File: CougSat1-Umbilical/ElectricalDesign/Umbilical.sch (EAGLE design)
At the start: 42 parts, among them J3 5V input, Q1 CSD16406Q3, Q2 CSD16406Q3, U1 FT230XQ, U2 BQ24650

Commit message: added test points
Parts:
- added TP1, TP2, TP3, TP4, TP5, TP6, TP7: TEST_POINT-THT-1.0, CougsInSpace-Connectors:TEST_POINT-THT-1.0
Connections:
- net 5.0V: now also TP1.1
- net BAT_CHARGE_OUT: now also TP4.1
- net DIODE_OUT: now also TP2.1
- net PH: now also TP3.1
- net USB5V: now also TP5.1
- net USB5V_FILTERED: now also TP6.1
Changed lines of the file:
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@@
 <?xml version="1.0" encoding="utf-8"?>
 <!DOCTYPE eagle SYSTEM "eagle.dtd">
-<eagle version="9.3.1">
+<eagle version="9.3.2">
 <drawing>
 <settings>
@@
 <part name="C8" library="CougsInSpace-Capacitors" deviceset="CAP-H" device="-1608" technology="-100NF" value="100nF 10%"/>
 <part name="SUPPLY7" library="CougsInSpace-PowerSymbols" deviceset="DGND" device=""/>
+<part name="TP1" library="CougsInSpace-Connectors" deviceset="TEST_POINT" device="-THT-1.0"/>
+<part name="TP2" library="CougsInSpace-Connectors" deviceset="TEST_POINT" device="-THT-1.0"/>
+<part name="TP3" library="CougsInSpace-Connectors" deviceset="TEST_POINT" device="-THT-1.0"/>
+<part name="TP4" library="CougsInSpace-Connectors" deviceset="TEST_POINT" device="-THT-1.0"/>
+<part name="TP5" library="CougsInSpace-Connectors" deviceset="TEST_POINT" device="-THT-1.0"/>
+<part name="TP6" library="CougsInSpace-Connectors" deviceset="TEST_POINT" device="-THT-1.0"/>
+<part name="TP7" library="CougsInSpace-Connectors" deviceset="TEST_POINT" device="-THT-1.0"/>
 </parts>
 <sheets>
@@
 <attribute name="SKU" x="186.69" y="106.68" size="1.27" layer="97" align="center"/>
 </instance>
+<instance part="TP1" gate="G$1" x="43.18" y="170.18" smashed="yes">
+<attribute name="NAME" x="41.656" y="171.704" size="1.27" layer="95" align="center"/>
+</instance>
+<instance part="TP2" gate="G$1" x="81.28" y="170.18" smashed="yes">
+<attribute name="NAME" x="79.756" y="171.704" size="1.27" layer="95" align="center"/>
+</instance>
+<instance part="TP3" gate="G$1" x="142.24" y="114.3" smashed="yes" rot="MR0">
+<attribute name="NAME" x="143.764" y="115.824" size="1.27" layer="95" rot="MR0" align="center"/>
+</instance>
+<instance part="TP4" gate="G$1" x="220.98" y="114.3" smashed="yes">
+<attribute name="NAME" x="219.456" y="115.824" size="1.27" layer="95" align="center"/>
+</instance>
 </instances>
 <busses>
@@
 <segment>
 <pinref part="D1" gate="G$1" pin="OUT"/>
-<wire x1="76.2" y1="167.64" x2="88.9" y2="167.64" width="0.1524" layer="91"/>
+<wire x1="76.2" y1="167.64" x2="83.82" y2="167.64" width="0.1524" layer="91"/>
 <pinref part="Q2" gate="G$1" pin="D"/>
+<wire x1="83.82" y1="167.64" x2="88.9" y2="167.64" width="0.1524" layer="91"/>
 <wire x1="88.9" y1="167.64" x2="116.84" y2="167.64" width="0.1524" layer="91"/>
 <wire x1="116.84" y1="167.64" x2="129.54" y2="167.64" width="0.1524" layer="91"/>
@@
 <pinref part="C9" gate="G$1" pin="1"/>
 <junction x="116.84" y="167.64"/>
+<pinref part="TP2" gate="G$1" pin="1"/>
+<wire x1="81.28" y1="170.18" x2="83.82" y2="170.18" width="0.1524" layer="91"/>
+<wire x1="83.82" y1="170.18" x2="83.82" y2="167.64" width="0.1524" layer="91"/>
+<junction x="83.82" y="167.64"/>
 </segment>
 </net>
@@
 <segment>
 <pinref part="D1" gate="G$1" pin="IN"/>
-<wire x1="33.02" y1="167.64" x2="55.88" y2="167.64" width="0.1524" layer="91"/>
+<wire x1="33.02" y1="167.64" x2="45.72" y2="167.64" width="0.1524" layer="91"/>
 <pinref part="SUPPLY4" gate="G$1" pin="5.0V"/>
+<wire x1="45.72" y1="167.64" x2="55.88" y2="167.64" width="0.1524" layer="91"/>
 <wire x1="33.02" y1="170.18" x2="33.02" y2="167.64" width="0.1524" layer="91"/>
 <junction x="33.02" y="167.64"/>
 <pinref part="J3" gate="G$1" pin="CENTER"/>
 <wire x1="30.48" y1="167.64" x2="33.02" y2="167.64" width="0.1524" layer="91"/>
+<pinref part="TP1" gate="G$1" pin="1"/>
+<wire x1="43.18" y1="170.18" x2="45.72" y2="170.18" width="0.1524" layer="91"/>
+<wire x1="45.72" y1="170.18" x2="45.72" y2="167.64" width="0.1524" layer="91"/>
+<junction x="45.72" y="167.64"/>
 </segment>
 <segment>
@@
 <pinref part="L1" gate="G$1" pin="1"/>
 <wire x1="129.54" y1="111.76" x2="129.54" y2="109.22" width="0.1524" layer="91"/>
-<wire x1="129.54" y1="111.76" x2="147.32" y2="111.76" width="0.1524" layer="91"/>
+<wire x1="129.54" y1="111.76" x2="139.7" y2="111.76" width="0.1524" layer="91"/>
 <junction x="129.54" y="111.76"/>
 <pinref part="U2" gate="G$1" pin="PH"/>
+<wire x1="139.7" y1="111.76" x2="147.32" y2="111.76" width="0.1524" layer="91"/>
 <wire x1="81.28" y1="111.76" x2="111.76" y2="111.76" width="0.1524" layer="91"/>
 <pinref part="C10" gate="G$1" pin="2"/>
@@
 <wire x1="111.76" y1="111.76" x2="111.76" y2="116.84" width="0.1524" layer="91"/>
 <junction x="111.76" y="111.76"/>
+<pinref part="TP3" gate="G$1" pin="1"/>
+<wire x1="142.24" y1="114.3" x2="139.7" y2="114.3" width="0.1524" layer="91"/>
+<wire x1="139.7" y1="114.3" x2="139.7" y2="111.76" width="0.1524" layer="91"/>
+<junction x="139.7" y="111.76"/>
 </segment>
 </net>
@@
 <pinref part="C14" gate="G$1" pin="1"/>
 <wire x1="208.28" y1="111.76" x2="213.36" y2="111.76" width="0.1524" layer="91"/>
-<wire x1="213.36" y1="111.76" x2="226.06" y2="111.76" width="0.1524" layer="91"/>
+<wire x1="213.36" y1="111.76" x2="223.52" y2="111.76" width="0.1524" layer="91"/>
+<wire x1="223.52" y1="111.76" x2="226.06" y2="111.76" width="0.1524" layer="91"/>
 <wire x1="226.06" y1="111.76" x2="238.76" y2="111.76" width="0.1524" layer="91"/>
 <wire x1="238.76" y1="111.76" x2="243.84" y2="111.76" width="0.1524" layer="91"/>
@@
 <junction x="238.76" y="111.76"/>
 <pinref part="R8" gate="G$1" pin="2"/>
+<pinref part="TP4" gate="G$1" pin="1"/>
+<wire x1="220.98" y1="114.3" x2="223.52" y2="114.3" width="0.1524" layer="91"/>
+<wire x1="223.52" y1="114.3" x2="223.52" y2="111.76" width="0.1524" layer="91"/>
+<junction x="223.52" y="111.76"/>
 </segment>
 </net>
@@
 </instance>
 <instance part="SUPPLY7" gate="1" x="149.86" y="86.36" smashed="yes"/>
+<instance part="TP5" gate="G$1" x="73.66" y="144.78" smashed="yes" rot="MR180">
+<attribute name="NAME" x="72.136" y="143.256" size="1.27" layer="95" rot="MR180" align="center"/>
+</instance>
+<instance part="TP6" gate="G$1" x="127" y="144.78" smashed="yes">
+<attribute name="NAME" x="125.476" y="146.304" size="1.27" layer="95" align="center"/>
+</instance>
+<instance part="TP7" gate="G$1" x="172.72" y="114.3" smashed="yes">
+<attribute name="NAME" x="171.196" y="115.824" size="1.27" layer="95" align="center"/>
+</instance>
 </instances>
 <busses>
@@
 <wire x1="137.16" y1="129.54" x2="134.62" y2="129.54" width="0.1524" layer="91"/>
 <pinref part="FB1" gate="G$1" pin="2"/>
-<wire x1="134.62" y1="142.24" x2="116.84" y2="142.24" width="0.1524" layer="91"/>
+<wire x1="134.62" y1="142.24" x2="129.54" y2="142.24" width="0.1524" layer="91"/>
+<wire x1="129.54" y1="142.24" x2="116.84" y2="142.24" width="0.1524" layer="91"/>
 <wire x1="116.84" y1="142.24" x2="101.6" y2="142.24" width="0.1524" layer="91"/>
 <wire x1="101.6" y1="142.24" x2="96.52" y2="142.24" width="0.1524" layer="91"/>
@@
 <junction x="101.6" y="142.24"/>
 <pinref part="C6" gate="G$1" pin="A"/>
+<pinref part="TP6" gate="G$1" pin="1"/>
+<wire x1="127" y1="144.78" x2="129.54" y2="144.78" width="0.1524" layer="91"/>
+<wire x1="129.54" y1="144.78" x2="129.54" y2="142.24" width="0.1524" layer="91"/>
+<junction x="129.54" y="142.24"/>
 </segment>
 </net>
@@
 <wire x1="71.12" y1="142.24" x2="71.12" y2="114.3" width="0.1524" layer="91"/>
 <junction x="76.2" y="142.24"/>
-</segment>
-</net>
+<pinref part="TP5" gate="G$1" pin="1"/>
+<wire x1="73.66" y1="144.78" x2="76.2" y2="144.78" width="0.1524" layer="91"/>
+<wire x1="76.2" y1="144.78" x2="76.2" y2="142.24" width="0.1524" layer="91"/>
+</segment>
+</net>

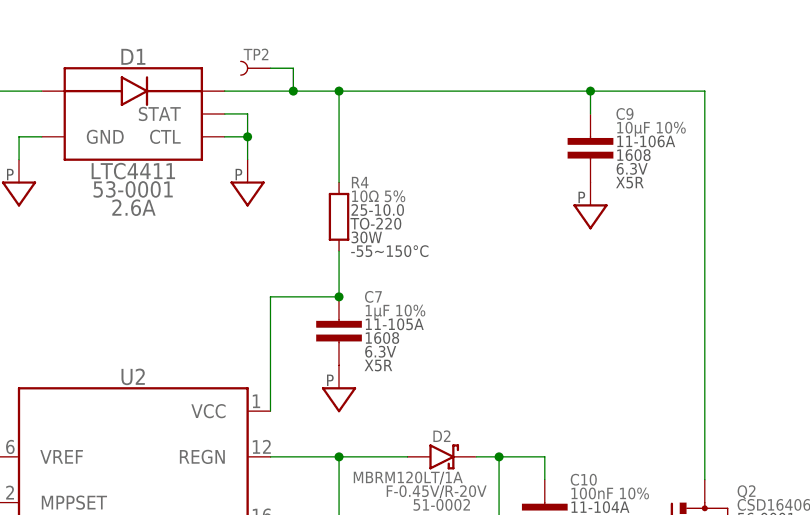
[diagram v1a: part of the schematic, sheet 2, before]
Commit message: fixed board outline
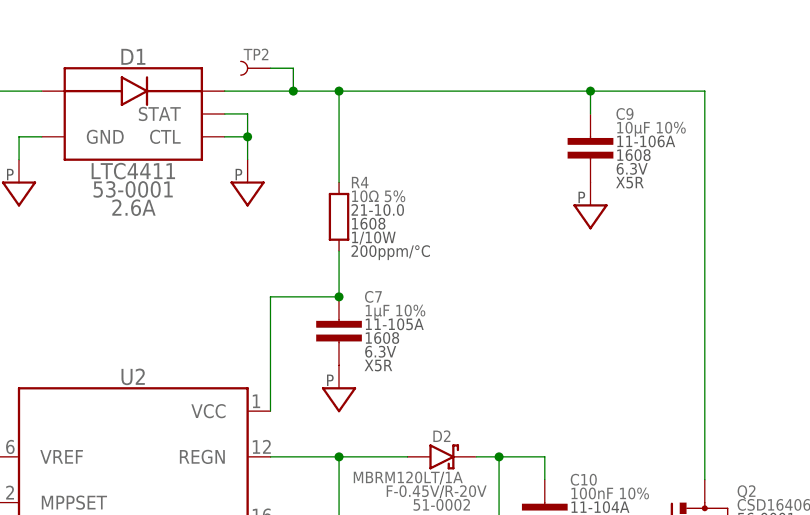
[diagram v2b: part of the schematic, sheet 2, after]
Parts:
- R4: device CougsInSpace-Resistors:RES-V-10R-TO220 -> CougsInSpace-Resistors:RES-V-10R-1608
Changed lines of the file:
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@@
 <grid distance="0.1" unitdist="inch" unit="inch" style="lines" multiple="1" display="no" altdistance="0.01" altunitdist="inch" altunit="inch"/>
 <layers>
-<layer number="1" name="Top" color="4" fill="1" visible="no" active="no"/>
-<layer number="2" name="Route2" color="1" fill="3" visible="no" active="no"/>
-<layer number="3" name="Route3" color="4" fill="3" visible="no" active="no"/>
-<layer number="4" name="Route4" color="1" fill="4" visible="no" active="no"/>
-<layer number="5" name="Route5" color="4" fill="4" visible="no" active="no"/>
-<layer number="6" name="Route6" color="1" fill="8" visible="no" active="no"/>
-<layer number="7" name="Route7" color="4" fill="8" visible="no" active="no"/>
-<layer number="8" name="Route8" color="1" fill="2" visible="no" active="no"/>
-<layer number="9" name="Route9" color="4" fill="2" visible="no" active="no"/>
-<layer number="10" name="Route10" color="1" fill="7" visible="no" active="no"/>
-<layer number="11" name="Route11" color="4" fill="7" visible="no" active="no"/>
-<layer number="12" name="Route12" color="1" fill="5" visible="no" active="no"/>
-<layer number="13" name="Route13" color="4" fill="5" visible="no" active="no"/>
-<layer number="14" name="Route14" color="1" fill="6" visible="no" active="no"/>
-<layer number="15" name="Route15" color="4" fill="6" visible="no" active="no"/>
-<layer number="16" name="Bottom" color="1" fill="1" visible="no" active="no"/>
-<layer number="17" name="Pads" color="2" fill="1" visible="no" active="no"/>
-<layer number="18" name="Vias" color="2" fill="1" visible="no" active="no"/>
-<layer number="19" name="Unrouted" color="6" fill="1" visible="no" active="no"/>
-<layer number="20" name="Dimension" color="24" fill="1" visible="no" active="no"/>
-<layer number="21" name="tPlace" color="7" fill="1" visible="no" active="no"/>
-<layer number="22" name="bPlace" color="7" fill="1" visible="no" active="no"/>
-<layer number="23" name="tOrigins" color="15" fill="1" visible="no" active="no"/>
-<layer number="24" name="bOrigins" color="15" fill="1" visible="no" active="no"/>
-<layer number="25" name="tNames" color="7" fill="1" visible="no" active="no"/>
-<layer number="26" name="bNames" color="7" fill="1" visible="no" active="no"/>
-<layer number="27" name="tValues" color="7" fill="1" visible="no" active="no"/>
-<layer number="28" name="bValues" color="7" fill="1" visible="no" active="no"/>
+<layer number="1" name="Top" color="4" fill="1" visible="yes" active="no"/>
+<layer number="2" name="Route2" color="16" fill="1" visible="yes" active="no"/>
+<layer number="3" name="Route3" color="17" fill="1" visible="yes" active="no"/>
+<layer number="4" name="Route4" color="18" fill="1" visible="yes" active="no"/>
+<layer number="5" name="Route5" color="19" fill="1" visible="yes" active="no"/>
+<layer number="6" name="Route6" color="25" fill="1" visible="yes" active="no"/>
+<layer number="7" name="Route7" color="26" fill="1" visible="yes" active="no"/>
+<layer number="8" name="Route8" color="27" fill="1" visible="yes" active="no"/>
+<layer number="9" name="Route9" color="28" fill="1" visible="yes" active="no"/>
+<layer number="10" name="Route10" color="29" fill="1" visible="yes" active="no"/>
+<layer number="11" name="Route11" color="30" fill="1" visible="yes" active="no"/>
+<layer number="12" name="Route12" color="20" fill="1" visible="yes" active="no"/>
+<layer number="13" name="Route13" color="21" fill="1" visible="yes" active="no"/>
+<layer number="14" name="Route14" color="22" fill="1" visible="yes" active="no"/>
+<layer number="15" name="Route15" color="23" fill="1" visible="yes" active="no"/>
+<layer number="16" name="Bottom" color="1" fill="1" visible="yes" active="no"/>
+<layer number="17" name="Pads" color="2" fill="1" visible="yes" active="no"/>
+<layer number="18" name="Vias" color="2" fill="1" visible="yes" active="no"/>
+<layer number="19" name="Unrouted" color="6" fill="1" visible="yes" active="no"/>
+<layer number="20" name="Dimension" color="24" fill="1" visible="yes" active="no"/>
+<layer number="21" name="tPlace" color="7" fill="1" visible="yes" active="no"/>
+<layer number="22" name="bPlace" color="7" fill="1" visible="yes" active="no"/>
+<layer number="23" name="tOrigins" color="15" fill="1" visible="yes" active="no"/>
+<layer number="24" name="bOrigins" color="15" fill="1" visible="yes" active="no"/>
+<layer number="25" name="tNames" color="7" fill="1" visible="yes" active="no"/>
+<layer number="26" name="bNames" color="7" fill="1" visible="yes" active="no"/>
+<layer number="27" name="tValues" color="7" fill="1" visible="yes" active="no"/>
+<layer number="28" name="bValues" color="7" fill="1" visible="yes" active="no"/>
 <layer number="29" name="tStop" color="7" fill="3" visible="no" active="no"/>
 <layer number="30" name="bStop" color="7" fill="6" visible="no" active="no"/>
@@
 <layer number="35" name="tGlue" color="7" fill="4" visible="no" active="no"/>
 <layer number="36" name="bGlue" color="7" fill="5" visible="no" active="no"/>
-<layer number="37" name="tTest" color="7" fill="1" visible="no" active="no"/>
-<layer number="38" name="bTest" color="7" fill="1" visible="no" active="no"/>
+<layer number="37" name="tTest" color="7" fill="1" visible="yes" active="no"/>
+<layer number="38" name="bTest" color="7" fill="1" visible="yes" active="no"/>
 <layer number="39" name="tKeepout" color="4" fill="11" visible="no" active="no"/>
 <layer number="40" name="bKeepout" color="1" fill="11" visible="no" active="no"/>
@@
 <layer number="44" name="Drills" color="7" fill="1" visible="no" active="no"/>
 <layer number="45" name="Holes" color="7" fill="1" visible="no" active="no"/>
-<layer number="46" name="Milling" color="3" fill="1" visible="no" active="no"/>
-<layer number="47" name="Measures" color="7" fill="1" visible="no" active="no"/>
-<layer number="48" name="Document" color="7" fill="1" visible="no" active="no"/>
-<layer number="49" name="Reference" color="7" fill="1" visible="no" active="no"/>
-<layer number="50" name="dxf" color="7" fill="1" visible="no" active="no"/>
-<layer number="51" name="tDocu" color="7" fill="1" visible="no" active="no"/>
-<layer number="52" name="bDocu" color="7" fill="1" visible="no" active="no"/>
-<layer number="53" name="tGND_GNDA" color="7" fill="9" visible="no" active="no"/>
-<layer number="54" name="bGND_GNDA" color="1" fill="9" visible="no" active="no"/>
-<layer number="56" name="wert" color="7" fill="1" visible="no" active="no"/>
-<layer number="57" name="tCAD" color="7" fill="1" visible="no" active="no"/>
-<layer number="58" name="bCAD" color="9" fill="1" visible="no" active="no"/>
-<layer number="59" name="tCarbon" color="7" fill="1" visible="no" active="no"/>
-<layer number="60" name="bCarbon" color="7" fill="1" visible="no" active="no"/>
+<layer number="46" name="Milling" color="3" fill="1" visible="yes" active="no"/>
+<layer number="47" name="Measures" color="7" fill="1" visible="yes" active="no"/>
+<layer number="48" name="Document" color="7" fill="1" visible="yes" active="no"/>
+<layer number="49" name="Reference" color="7" fill="1" visible="yes" active="no"/>
+<layer number="50" name="dxf" color="7" fill="1" visible="yes" active="no"/>
+<layer number="51" name="tDocu" color="7" fill="1" visible="yes" active="no"/>
+<layer number="52" name="bDocu" color="7" fill="1" visible="yes" active="no"/>
+<layer number="53" name="tGND_GNDA" color="7" fill="9" visible="yes" active="no"/>
+<layer number="54" name="bGND_GNDA" color="1" fill="9" visible="yes" active="no"/>
+<layer number="56" name="wert" color="7" fill="1" visible="yes" active="no"/>
+<layer number="57" name="tCAD" color="7" fill="1" visible="yes" active="no"/>
+<layer number="58" name="bCAD" color="9" fill="1" visible="yes" active="no"/>
+<layer number="59" name="tCarbon" color="7" fill="1" visible="yes" active="no"/>
+<layer number="60" name="bCarbon" color="7" fill="1" visible="yes" active="no"/>
 <layer number="88" name="SimResults" color="9" fill="1" visible="yes" active="yes"/>
 <layer number="89" name="SimProbes" color="9" fill="1" visible="yes" active="yes"/>
@@
 <part name="R11" library="CougsInSpace-Resistors" deviceset="RES-V" device="-1608" technology="-2.2K" value="2.2kΩ 1%"/>
 <part name="R12" library="CougsInSpace-Resistors" deviceset="RES-V" device="-1608" technology="-3.3K" value="3.3kΩ 0.1%"/>
-<part name="R4" library="CougsInSpace-Resistors" deviceset="RES-V" device="-TO220" technology="-10R" value="10Ω 5%"/>
+<part name="R4" library="CougsInSpace-Resistors" deviceset="RES-V" device="-1608" technology="-10R" value="10Ω 5%"/>
 <part name="SUPPLY28" library="CougsInSpace-PowerSymbols" deviceset="5.0V" device=""/>
 <part name="C16" library="CougsInSpace-Capacitors" deviceset="CAP-H" device="-1608" technology="-100NF" value="100nF 10%"/>
